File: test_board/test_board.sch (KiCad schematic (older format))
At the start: 57 parts, among them J1 Screw_Terminal_01x02, J2 USB_B_Micro, J3 I2C1, J4 USART2, J5 SWD, J6 USART6, J7 CAN1, J8 USART3, Q1 AO3401A, SW1 SW_SPDT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

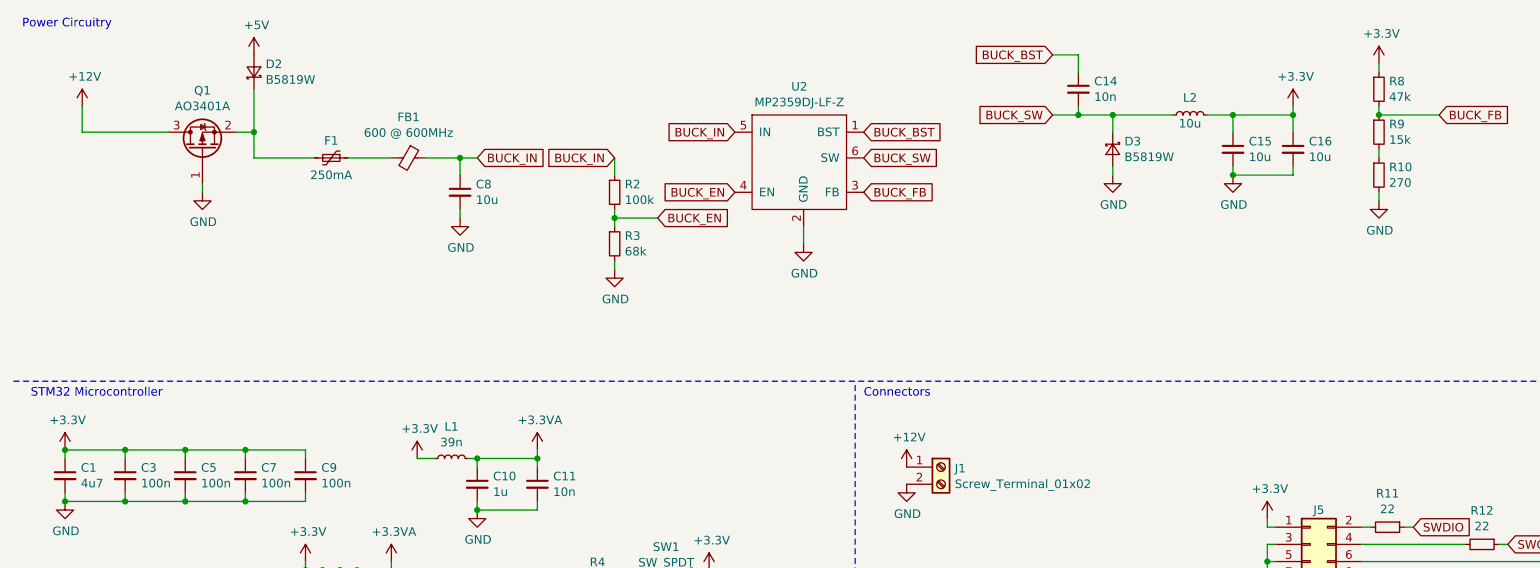
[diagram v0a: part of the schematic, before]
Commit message: Replace MD3579DJ with LM2576-ADJ
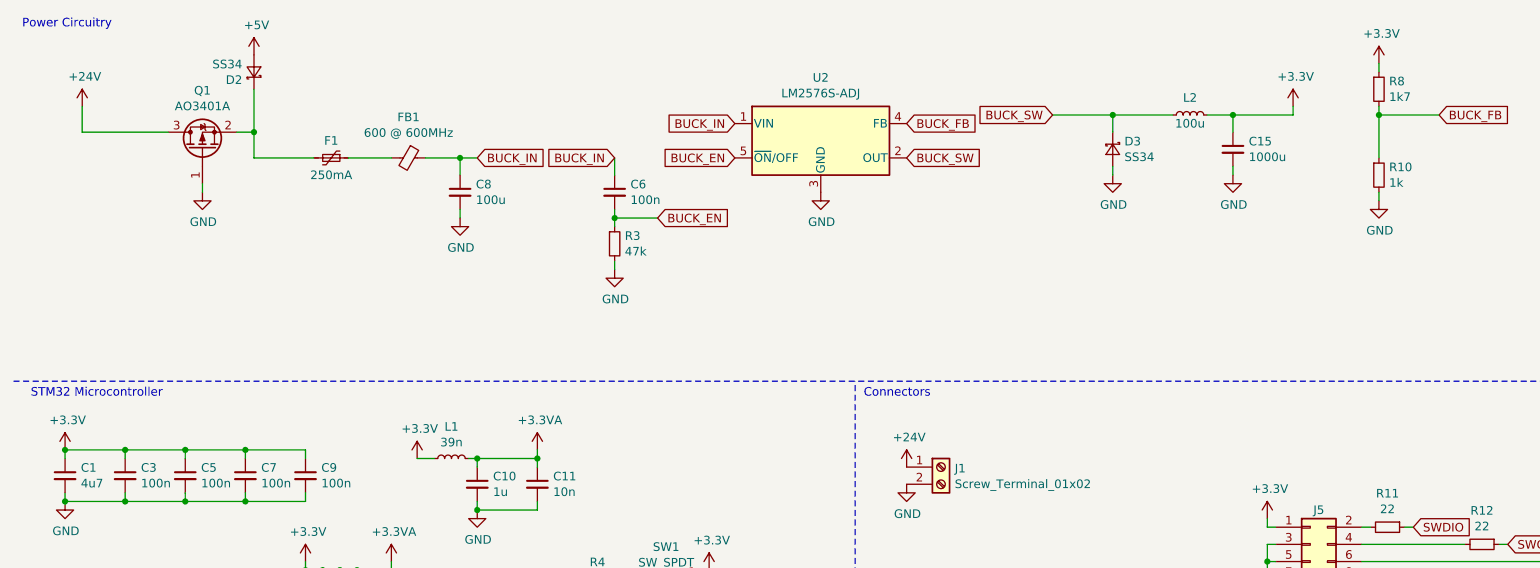
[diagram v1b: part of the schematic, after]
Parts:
- removed C14: 10n, Capacitor_SMD:C_1206_3216Metric, symbol Device:C_Small
- removed C16: 10u, Capacitor_SMD:C_1206_3216Metric, symbol Device:C_Small
- removed R2: 100k, Resistor_SMD:R_0603_1608Metric, symbol Device:R_Small
- removed R9: 15k, Resistor_SMD:R_0603_1608Metric, symbol Device:R_Small
- removed U2: MP2359DJ-LF-Z, MyKiCADFootprints:SOIC127P599X175-8N, symbol MyKiCADLibrary:MP2359DJ-LF-Z
- added C6: 100n, Capacitor_SMD:C_1206_3216Metric, symbol Device:C_Small
- added U2: LM2576S-ADJ, Package_TO_SOT_SMD:TO-263-5_TabPin3, symbol Regulator_Switching:LM2576S-ADJ
- C1: LCSC Part # C19666 -> C19666
- C15: value 10u -> 1000u
- C3, C5, C7, C9: LCSC Part # C1525 -> C1525
- C8, L2: value 10u -> 100u
- D2, D3: value B5819W -> SS34; footprint Diode_SMD:D_SOD-123 -> Diode_SMD:D_SMC
- R10: value 270 -> 1k
- R3: value 68k -> 47k
- R8: value 47k -> 1k7
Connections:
- net BUCK_EN: now also C6.2, U2.5 (~ON~/OFF)
- net BUCK_FB: now also R10.1, U2.4 (FB)
- net BUCK_IN: now also C6.1, U2.1 (VIN)
- net BUCK_SW: now also U2.2 (OUT)
- net GND: now also U2.3 (GND)
- net +12V renamed +24V
